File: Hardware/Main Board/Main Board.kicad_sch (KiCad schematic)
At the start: 85 parts, among them J1 Micro_SD_Card_Det1, J3 Conn_01x09_Socket, J4 MIC 1 Connector, J5 MIC 2 Connector, J6 USB_C_Receptacle_USB2.0_16P, J7 OLED, Q1 AO3401A, SW1 SW_SPST, U1 ESP32-S3-WROOM-2, U2 TPS63060, U3 TP4056-42-ESOP8, U4 TLV75528PDBV, U6 AP2112K-1.2

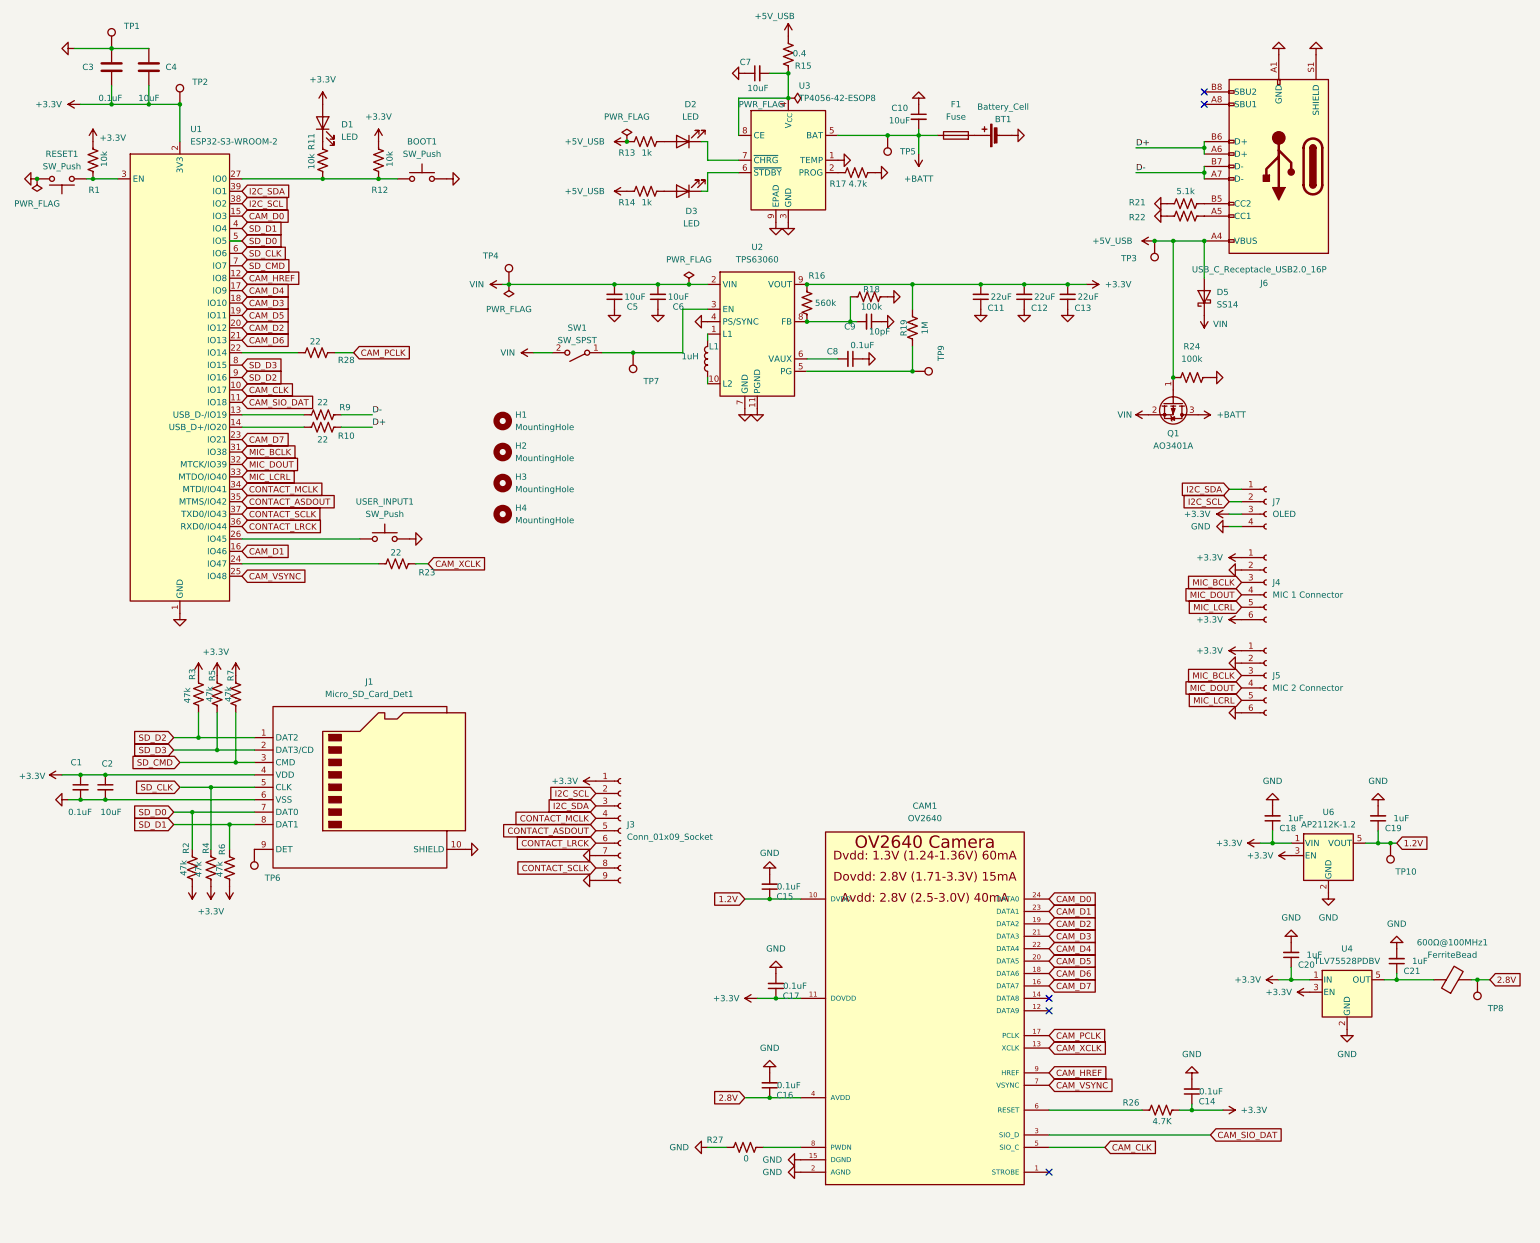
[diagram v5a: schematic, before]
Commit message: fixed data 0 and data 1 no connect issue, data pins for camera start at D2-D9
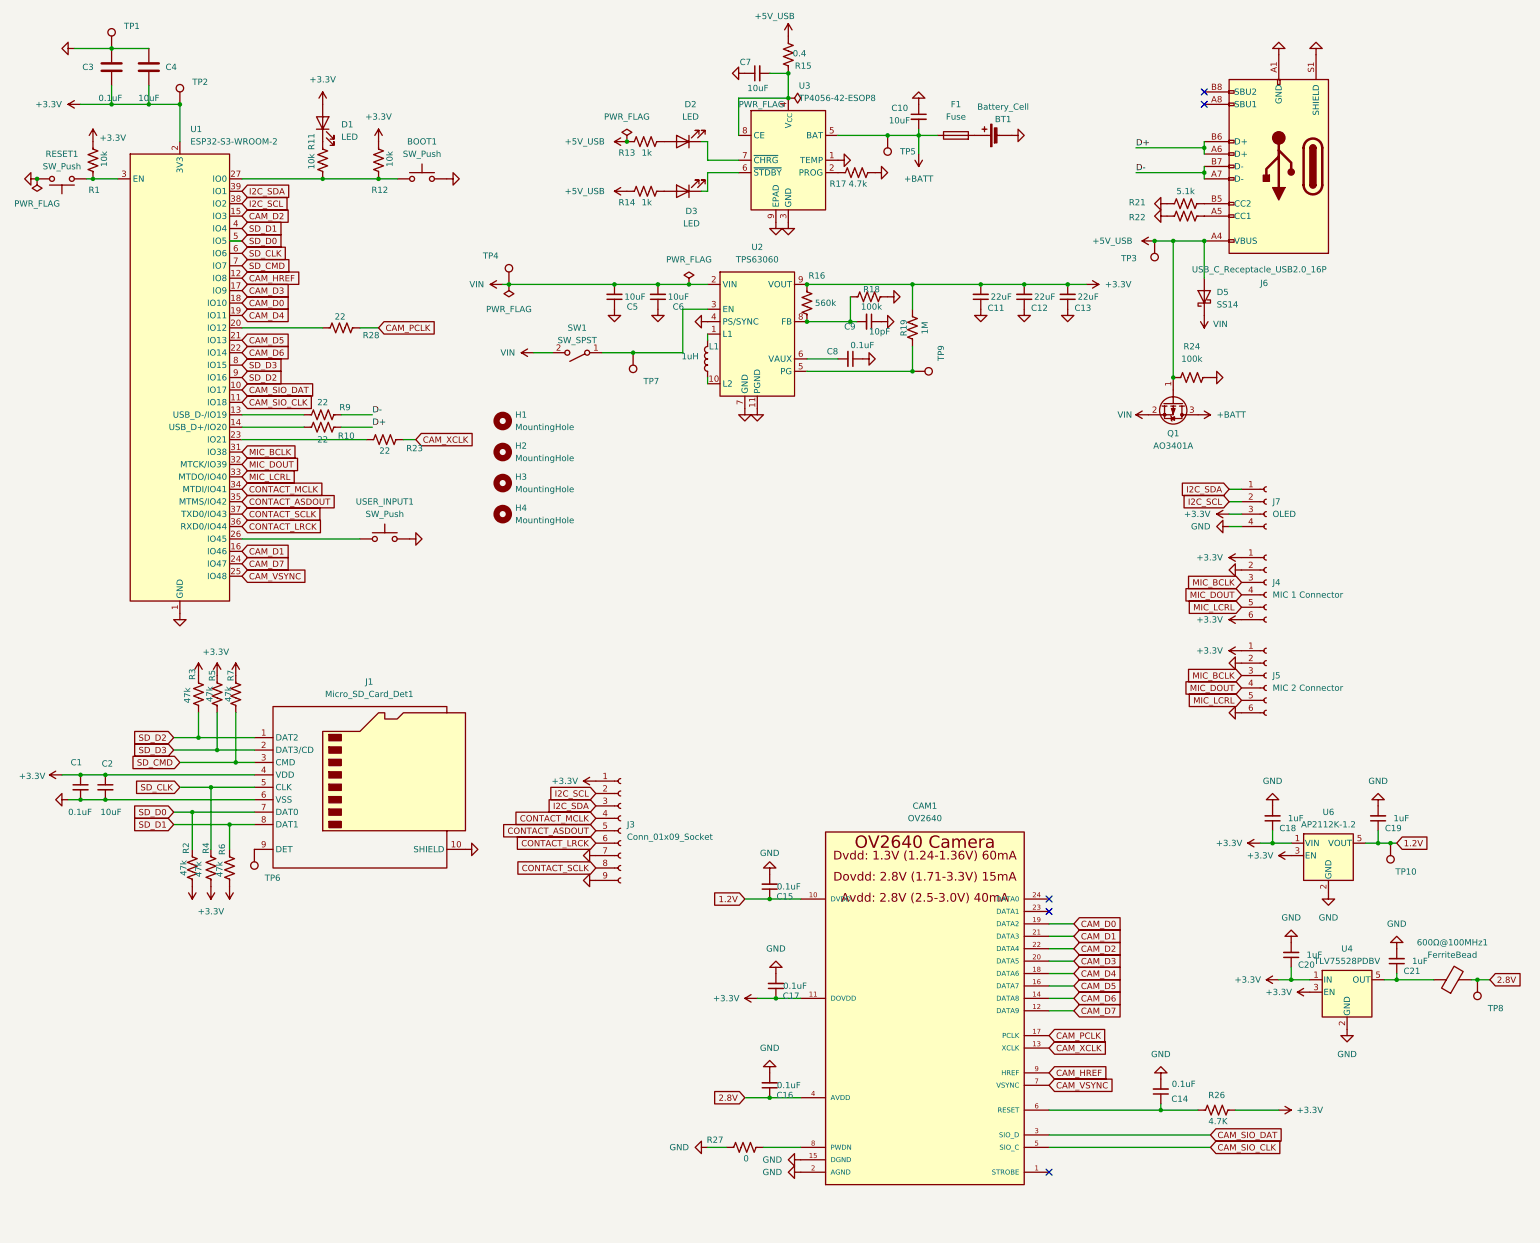
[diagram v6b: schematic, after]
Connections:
- net +3.3V: no longer C14.1
- net CAM_D0: now also CAM1.19 (DATA2), U1.18 (IO10); no longer CAM1.24 (DATA0), U1.15 (IO3)
- net CAM_D1: now also CAM1.21 (DATA3); no longer CAM1.23 (DATA1)
- net CAM_D2: now also CAM1.22 (DATA4), U1.15 (IO3); no longer CAM1.19 (DATA2), U1.20 (IO12)
- net CAM_D3: now also CAM1.20 (DATA5), U1.17 (IO9); no longer CAM1.21 (DATA3), U1.18 (IO10)
- net CAM_D4: now also CAM1.18 (DATA6), U1.19 (IO11); no longer CAM1.22 (DATA4), U1.17 (IO9)
- net CAM_D5: now also CAM1.16 (DATA7), U1.21 (IO13); no longer CAM1.20 (DATA5), U1.19 (IO11)
- net CAM_D6: now also CAM1.14 (DATA8), U1.22 (IO14); no longer CAM1.18 (DATA6), U1.21 (IO13)
- net CAM_D7: now also CAM1.12 (DATA9), U1.24 (IO47); no longer CAM1.16 (DATA7), U1.23 (IO21)
- net CAM_SIO_DAT: now also U1.10 (IO17); no longer U1.11 (IO18)
- net at R28.1: now also U1.20 (IO12); no longer U1.22 (IO14)
- net at R23.1: now also U1.23 (IO21); no longer U1.24 (IO47)
- net at CAM1.6 (RESET), R26.2: now also C14.1
- net CAM_CLK renamed CAM_SIO_CLK
- net CAM_SIO_CLK: now also U1.11 (IO18); no longer U1.10 (IO17)
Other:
- moved on the sheet: C14, R23, R26, R28

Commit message: Pull hardware updates from codex temp branch
Bring the main board hardware changes from origin/codex-temp-main-hardware-push onto main while excluding transient KiCad autosave and lock files.
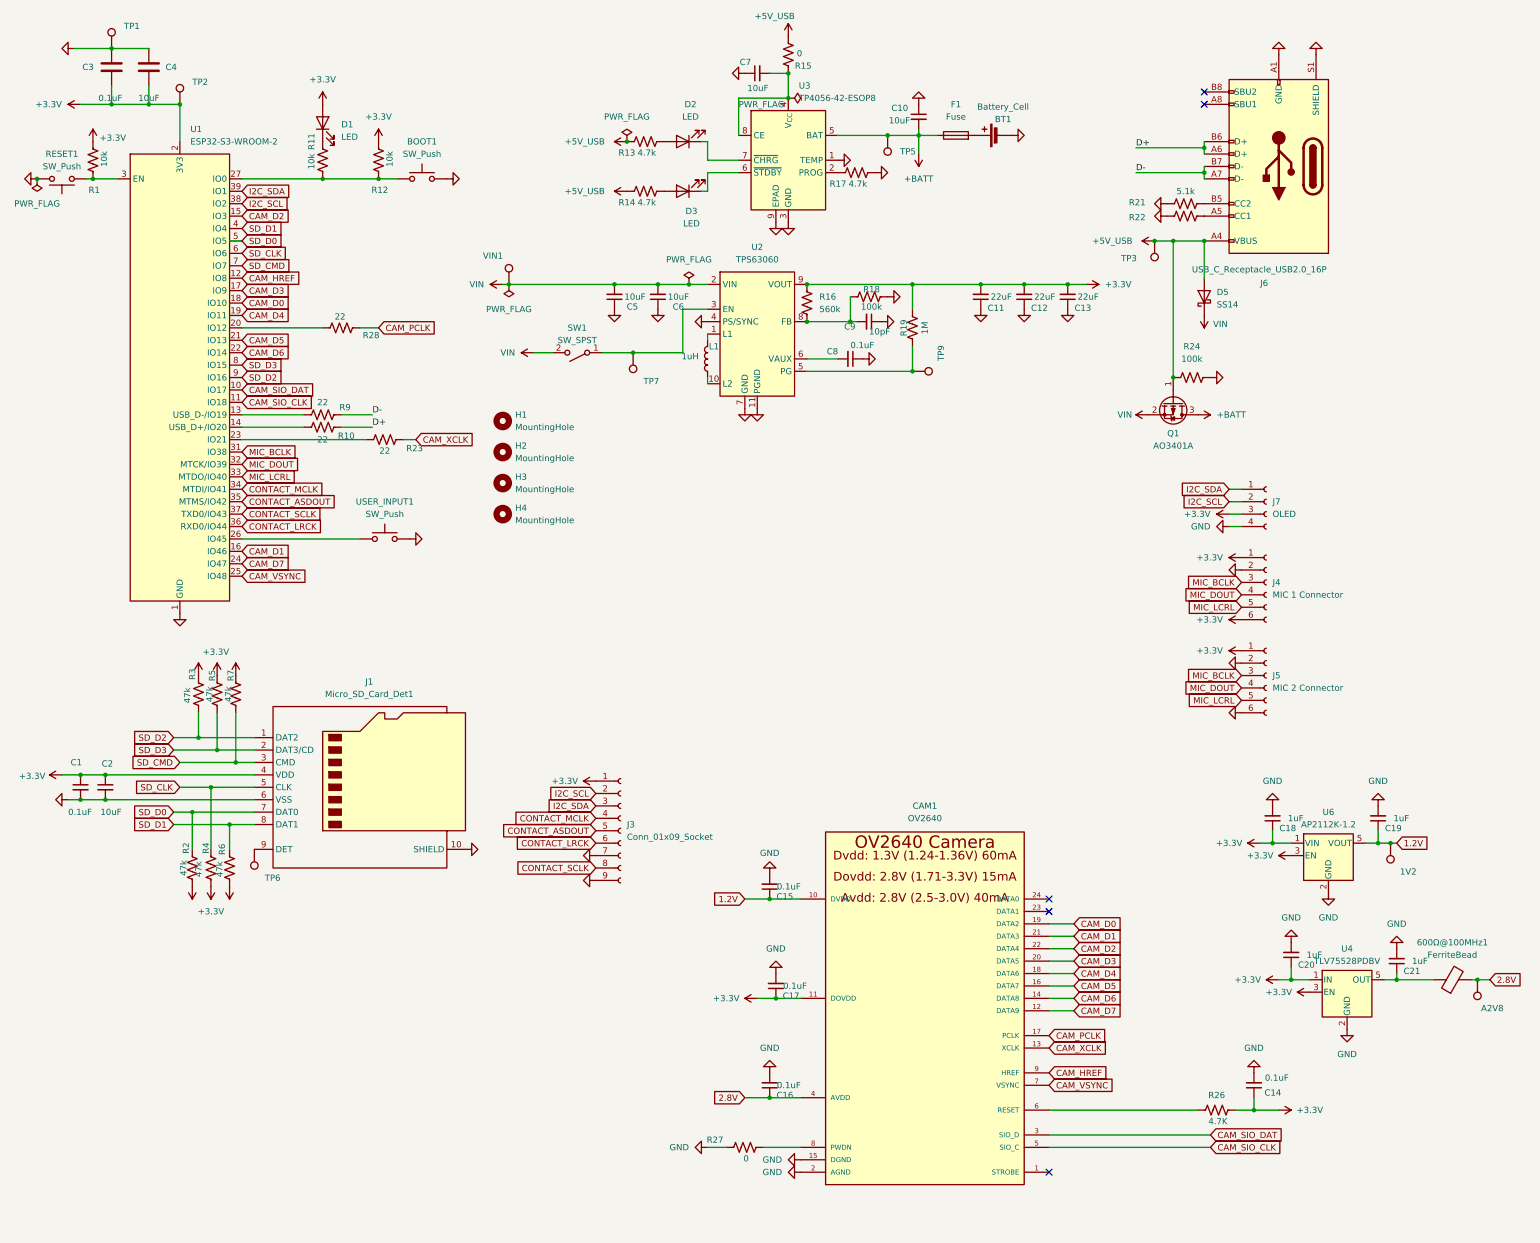
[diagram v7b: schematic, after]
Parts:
- BOOT1, RESET1: footprint Button_Switch_SMD:SW_Tactile_SPST_NO_Straight_CK_PTS636Sx25SMTRLFS -> Button_Switch_SMD:SW_SPST_TL3342
- D1: footprint Connector_PinHeader_2.00mm:PinHeader_1x02_P2.00mm_Vertical -> LED_SMD:LED_0603_1608Metric
- R13, R14: value 1k -> 4.7k
- R15: value 0.4 -> 0
- renumbered TP10 to 1V2, TP8 to A2V8, TP4 to VIN1
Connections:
- net +3.3V: now also C14.1
- net at CAM1.6 (RESET), R26.2: no longer C14.1
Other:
- moved on the sheet: C14
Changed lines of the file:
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@@
 	)
 	(junction
-		(at 260.35 242.57)
-		(diameter 0)
-		(color 0 0 0 0)
-	)
-	(junction
 		(at 63.5 166.37)
 		(diameter 0)
@@
 	)
 	(junction
+		(at 279.4 242.57)
+		(diameter 0)
+		(color 0 0 0 0)
+	)
+	(junction
 		(at 259.08 64.77)
 		(diameter 0)
@@
 	(wire
 		(pts
-			(xy 275.59 242.57) (xy 284.48 242.57)
+			(xy 275.59 242.57) (xy 279.4 242.57)
 		)
 		(stroke
@@
 	(wire
 		(pts
-			(xy 260.35 241.3) (xy 260.35 242.57)
+			(xy 279.4 240.03) (xy 279.4 242.57)
 		)
 		(stroke
@@
 	(wire
 		(pts
-			(xy 260.35 242.57) (xy 237.49 242.57)
+			(xy 237.49 242.57) (xy 267.97 242.57)
 		)
 		(stroke
@@
 	(wire
 		(pts
-			(xy 187.96 73.66) (xy 209.55 73.66)
+			(xy 279.4 242.57) (xy 284.48 242.57)
 		)
 		(stroke
@@
 	(wire
 		(pts
-			(xy 85.09 102.87) (xy 72.39 102.87)
+			(xy 187.96 73.66) (xy 209.55 73.66)
 		)
 		(stroke
@@
 	(wire
 		(pts
-			(xy 187.96 81.28) (xy 196.85 81.28)
+			(xy 85.09 102.87) (xy 72.39 102.87)
 		)
 		(stroke
@@
 	(wire
 		(pts
-			(xy 255.27 50.8) (xy 269.24 50.8)
+			(xy 187.96 81.28) (xy 196.85 81.28)
 		)
 		(stroke
@@
 	(wire
 		(pts
-			(xy 196.85 76.2) (xy 196.85 81.28)
+			(xy 255.27 50.8) (xy 269.24 50.8)
 		)
 		(stroke
@@
 	(wire
 		(pts
-			(xy 242.57 214.63) (xy 237.49 214.63)
+			(xy 196.85 76.2) (xy 196.85 81.28)
 		)
 		(stroke
@@
 	(wire
 		(pts
-			(xy 194.31 43.18) (xy 204.47 43.18)
+			(xy 242.57 214.63) (xy 237.49 214.63)
 		)
 		(stroke
@@
 	(wire
 		(pts
-			(xy 242.57 207.01) (xy 237.49 207.01)
+			(xy 194.31 43.18) (xy 204.47 43.18)
 		)
 		(stroke
@@
 	(wire
 		(pts
-			(xy 260.35 242.57) (xy 267.97 242.57)
+			(xy 242.57 207.01) (xy 237.49 207.01)
 		)
 		(stroke
@@
 		(on_board yes)
 		(dnp no)
+		(fields_autoplaced yes)
 		(property "Reference" "R16"
-			(at 189.992 71.882 0)
+			(at 190.5 76.1999 0)
 			(effects
 				(font
 					(size 1.27 1.27)
 				)
+				(justify right)
 			)
 		)
 		(property "Value" "560k"
-			(at 191.77 77.47 0)
+			(at 190.5 78.7399 0)
 			(effects
 				(font
 					(size 1.27 1.27)
 				)
+				(justify right)
 			)
 		)
@@
 			)
 		)
-		(property "Value" "1k"
+		(property "Value" "4.7k"
 			(at 155.194 46.736 90)
 			(effects
@@
 		(on_board yes)
 		(dnp no)
-		(property "Reference" "TP10"
+		(property "Reference" "1V2"
 			(at 312.674 193.802 0)
 			(effects
@@
 			(project "Main Board"
 				(path "/06300a21-1646-41b0-b473-1c39557d6dab"
-					(reference "TP10")
+					(reference "1V2")
 					(unit 1)
 				)
@@
 		(on_board yes)
 		(dnp no)
-		(property "Reference" "TP4"
+		(property "Reference" "VIN1"
 			(at 121.666 67.818 0)
 			(effects
@@
 			(project "Main Board"
 				(path "/06300a21-1646-41b0-b473-1c39557d6dab"
-					(reference "TP4")
+					(reference "VIN1")
 					(unit 1)
 				)
@@
 			)
 		)
-		(property "Value" "0.4"
+		(property "Value" "0"
 			(at 186.436 26.416 0)
 			(effects
@@
 	(symbol
 		(lib_id "Device:C_Small")
-		(at 260.35 238.76 180)
+		(at 279.4 237.49 180)
 		(unit 1)
 		(exclude_from_sim no)
@@
 		(dnp no)
 		(property "Reference" "C14"
-			(at 265.938 240.284 0)
+			(at 284.988 239.014 0)
 			(effects
 				(font
@@
 		)
 		(property "Value" "0.1uF"
-			(at 267.462 237.236 0)
+			(at 286.512 235.966 0)
 			(effects
 				(font
@@
 		)
 		(property "Footprint" "Capacitor_SMD:C_0603_1608Metric"
-			(at 260.35 238.76 0)
+			(at 279.4 237.49 0)
 			(effects
 				(font
@@
 		)
 		(property "Datasheet" "~"
-			(at 260.35 238.76 0)
+			(at 279.4 237.49 0)
 			(effects
 				(font
@@
 		)
 		(property "Description" "Unpolarized capacitor, small symbol"
-			(at 260.35 238.76 0)
+			(at 279.4 237.49 0)
 			(effects
 				(font
@@
 			)
 		)
-		(property "Footprint" "Connector_PinHeader_2.00mm:PinHeader_1x02_P2.00mm_Vertical"
+		(property "Footprint" "LED_SMD:LED_0603_1608Metric"
 			(at 88.9 40.64 0)
 			(effects
@@
 			)
 		)
-		(property "Value" "1k"
+		(property "Value" "4.7k"
 			(at 155.194 56.896 90)
 			(effects
@@
 		(on_board yes)
 		(dnp no)
-		(property "Reference" "TP8"
+		(property "Reference" "A2V8"
 			(at 330.454 221.742 0)
 			(effects
@@
 			(project "Main Board"
 				(path "/06300a21-1646-41b0-b473-1c39557d6dab"
-					(reference "TP8")
+					(reference "A2V8")
 					(unit 1)
 				)
@@
 			)
 		)
-		(property "Footprint" "Button_Switch_SMD:SW_Tactile_SPST_NO_Straight_CK_PTS636Sx25SMTRLFS"
+		(property "Footprint" "Button_Switch_SMD:SW_SPST_TL3342"
 			(at 35.56 57.15 0)
 			(effects
@@
 			)
 		)
-		(property "Footprint" "Button_Switch_SMD:SW_Tactile_SPST_NO_Straight_CK_PTS636Sx25SMTRLFS"
+		(property "Footprint" "Button_Switch_SMD:SW_SPST_TL3342"
 			(at 109.22 46.99 0)
 			(effects
@@
 	(symbol
 		(lib_id "power:GND")
-		(at 260.35 236.22 180)
+		(at 279.4 234.95 180)
 		(unit 1)
 		(exclude_from_sim no)
@@
 		(fields_autoplaced yes)
 		(property "Reference" "#PWR077"
-			(at 260.35 229.87 0)
+			(at 279.4 228.6 0)
 			(effects
 				(font
@@
 		)
 		(property "Value" "GND"
-			(at 260.35 231.14 0)
+			(at 279.4 229.87 0)
 			(effects
 				(font
@@
 		)
 		(property "Footprint" ""
-			(at 260.35 236.22 0)
+			(at 279.4 234.95 0)
 			(effects
 				(font
@@
 		)
 		(property "Datasheet" ""
-			(at 260.35 236.22 0)
+			(at 279.4 234.95 0)
 			(effects
 				(font
@@
 		)
 		(property "Description" "Power symbol creates a global label with name \"GND\" , ground"
-			(at 260.35 236.22 0)
+			(at 279.4 234.95 0)
 			(effects
 				(font
